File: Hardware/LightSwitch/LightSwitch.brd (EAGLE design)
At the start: 70.1 x 70 mm, 18 parts, among them IC1 ATMEGA328P, Q1 8MHz, X1 MAINS

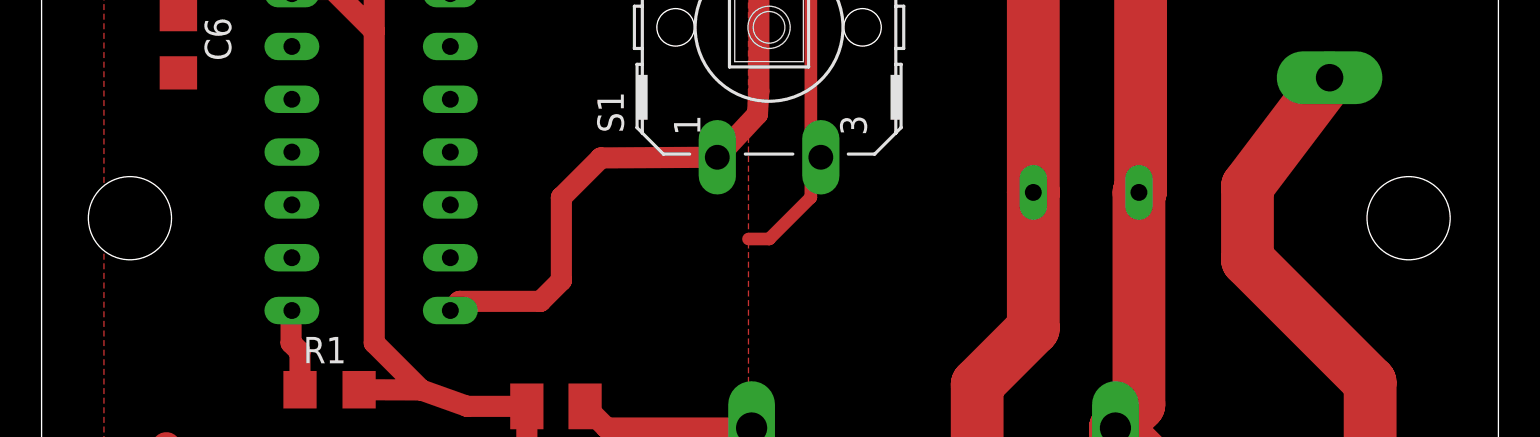
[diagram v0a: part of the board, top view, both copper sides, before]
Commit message: added mounting holes to include extra detail for silk
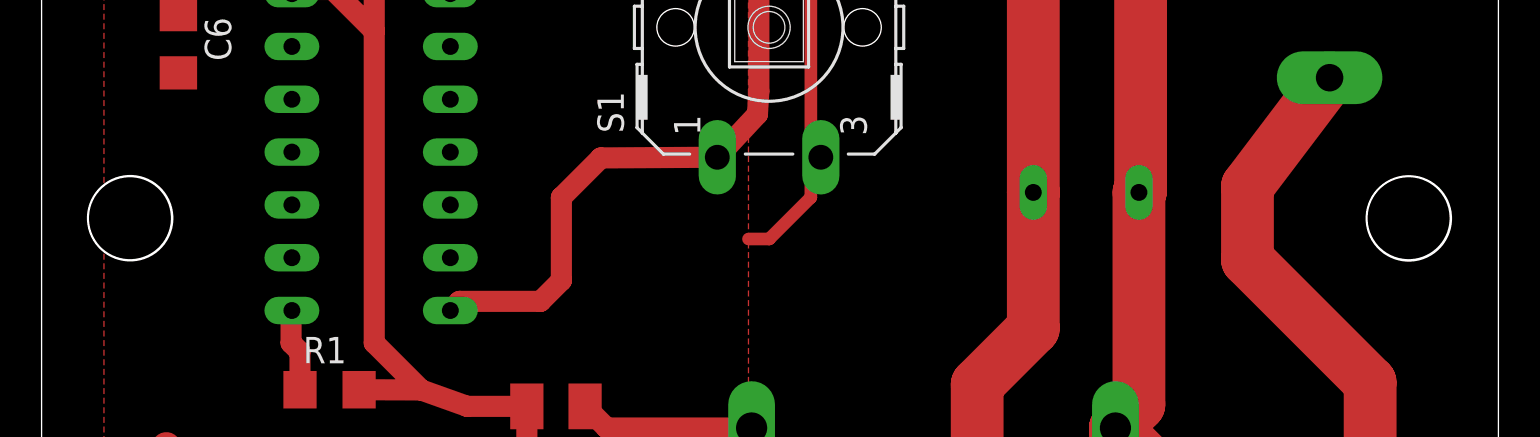
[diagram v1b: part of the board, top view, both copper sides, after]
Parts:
- added H1, H2: MOUNT-HOLE4.1, holes:4,1
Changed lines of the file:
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@@
 <setting verticaltext="up"/>
 </settings>
-<grid distance="1" unitdist="mm" unit="mm" style="lines" multiple="1" display="no" altdistance="0.1" altunitdist="mm" altunit="mm"/>
+<grid distance="1" unitdist="mm" unit="mm" style="lines" multiple="1" display="no" altdistance="0.01" altunitdist="mm" altunit="mm"/>
 <layers>
 <layer number="1" name="Top" color="4" fill="1" visible="yes" active="yes"/>
@@
 <layer number="23" name="tOrigins" color="15" fill="1" visible="yes" active="yes"/>
 <layer number="24" name="bOrigins" color="15" fill="1" visible="yes" active="yes"/>
-<layer number="25" name="tNames" color="7" fill="1" visible="yes" active="yes"/>
-<layer number="26" name="bNames" color="7" fill="1" visible="yes" active="yes"/>
+<layer number="25" name="tNames" color="7" fill="1" visible="no" active="yes"/>
+<layer number="26" name="bNames" color="7" fill="1" visible="no" active="yes"/>
 <layer number="27" name="tValues" color="7" fill="1" visible="no" active="yes"/>
 <layer number="28" name="bValues" color="7" fill="1" visible="no" active="yes"/>
@@
 <layer number="43" name="vRestrict" color="2" fill="10" visible="no" active="yes"/>
 <layer number="44" name="Drills" color="7" fill="1" visible="no" active="yes"/>
-<layer number="45" name="Holes" color="7" fill="1" visible="yes" active="yes"/>
+<layer number="45" name="Holes" color="7" fill="1" visible="no" active="yes"/>
 <layer number="46" name="Milling" color="3" fill="1" visible="no" active="yes"/>
 <layer number="47" name="Measures" color="7" fill="1" visible="no" active="yes"/>
 <layer number="48" name="Document" color="7" fill="1" visible="yes" active="yes"/>
 <layer number="49" name="Reference" color="7" fill="1" visible="yes" active="yes"/>
-<layer number="51" name="tDocu" color="7" fill="1" visible="no" active="yes"/>
-<layer number="52" name="bDocu" color="7" fill="1" visible="no" active="yes"/>
+<layer number="51" name="tDocu" color="7" fill="1" visible="yes" active="yes"/>
+<layer number="52" name="bDocu" color="7" fill="1" visible="yes" active="yes"/>
 <layer number="91" name="Nets" color="2" fill="1" visible="no" active="no"/>
 <layer number="92" name="Busses" color="1" fill="1" visible="no" active="no"/>
@@
 <element name="C6" library="rcl" package="C1206" value="22p" x="6.58" y="43.39" rot="R270"/>
 <element name="C7" library="rcl" package="C1206" value="22p" x="5.38" y="59.41" rot="R90"/>
+<element name="H1" library="holes" package="4,1" value="MOUNT-HOLE4.1" x="4.26" y="35" rot="MR0"/>
+<element name="H2" library="holes" package="4,1" value="MOUNT-HOLE4.1" x="65.76" y="34.99" rot="MR0"/>
 </elements>
 <signals>
